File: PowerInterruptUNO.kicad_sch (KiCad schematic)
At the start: 47 parts, among them J1 Power, J10 6P6C, J11 USB_C_Receptacle_USB2.0, J12 Screw_Terminal_01x02, J13 USB_A, J14 Screw_Terminal_01x02, J2 Analog, J3 Barrel_Jack_Switch, J4 Screw_Terminal_01x06, J5 Screw_Terminal_01x06, J6 Screw_Terminal_01x03, J7 Screw_Terminal_01x02, J8 Digital/PWM, J9 Digital/PWM, Q1 MMBT3904, Q2 TIP42, U1 LM317_TO-220

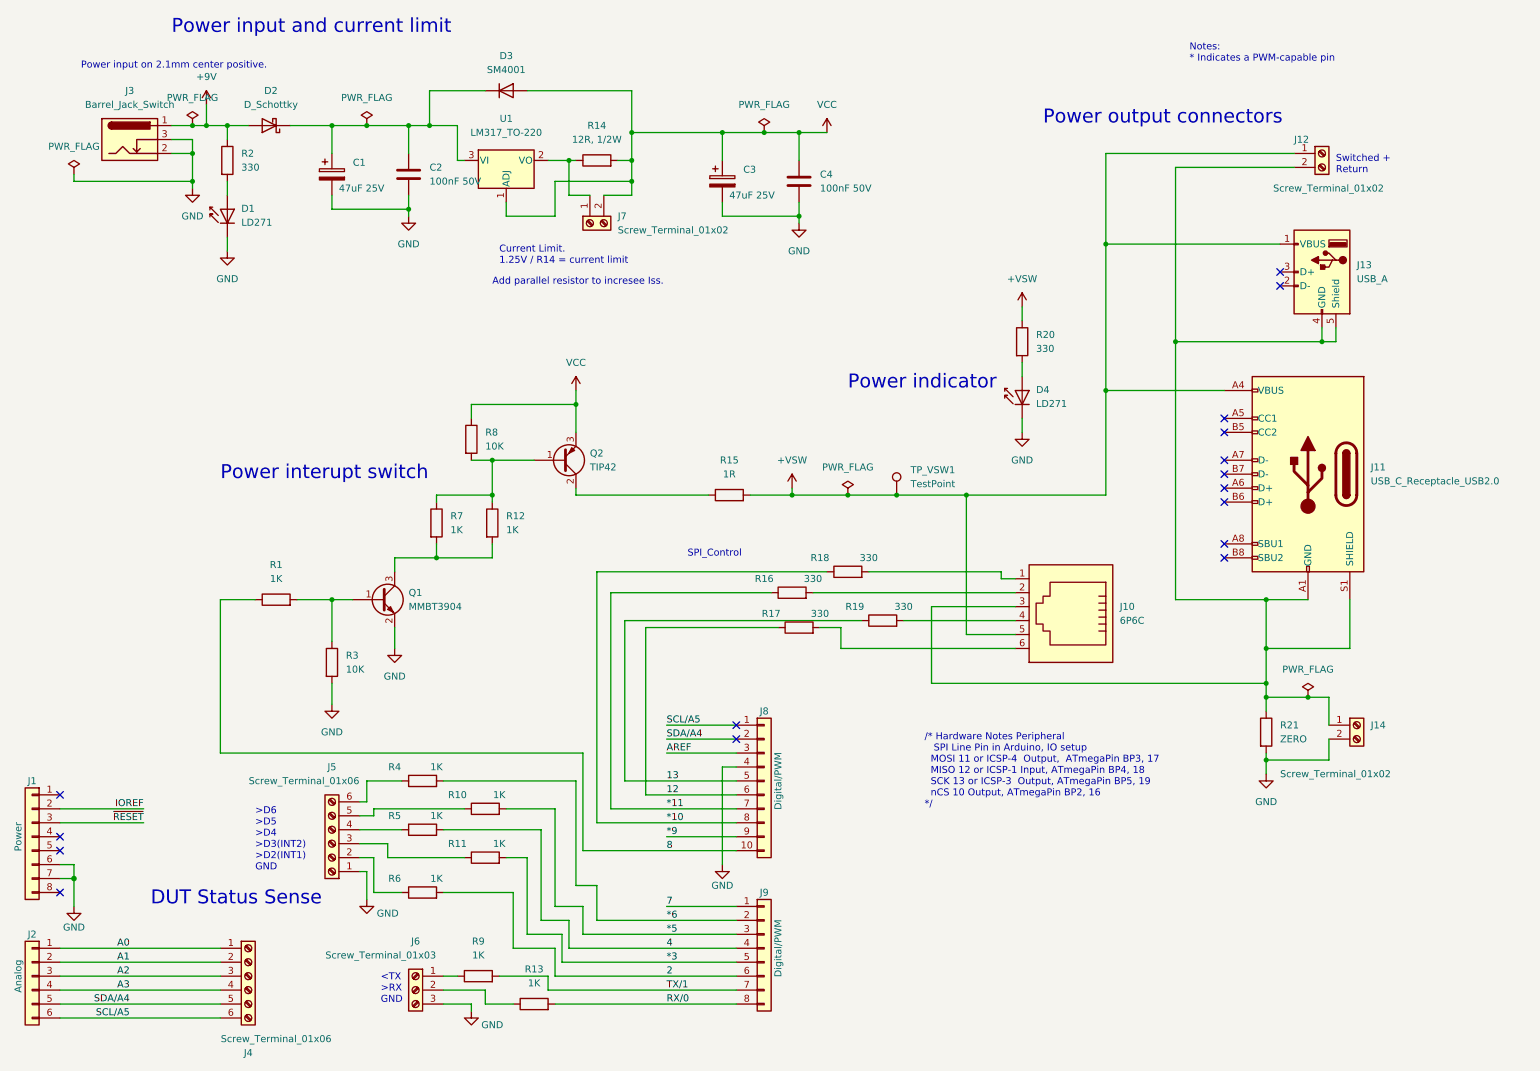
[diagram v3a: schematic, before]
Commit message: Add JLCPCB part numberes to some components.
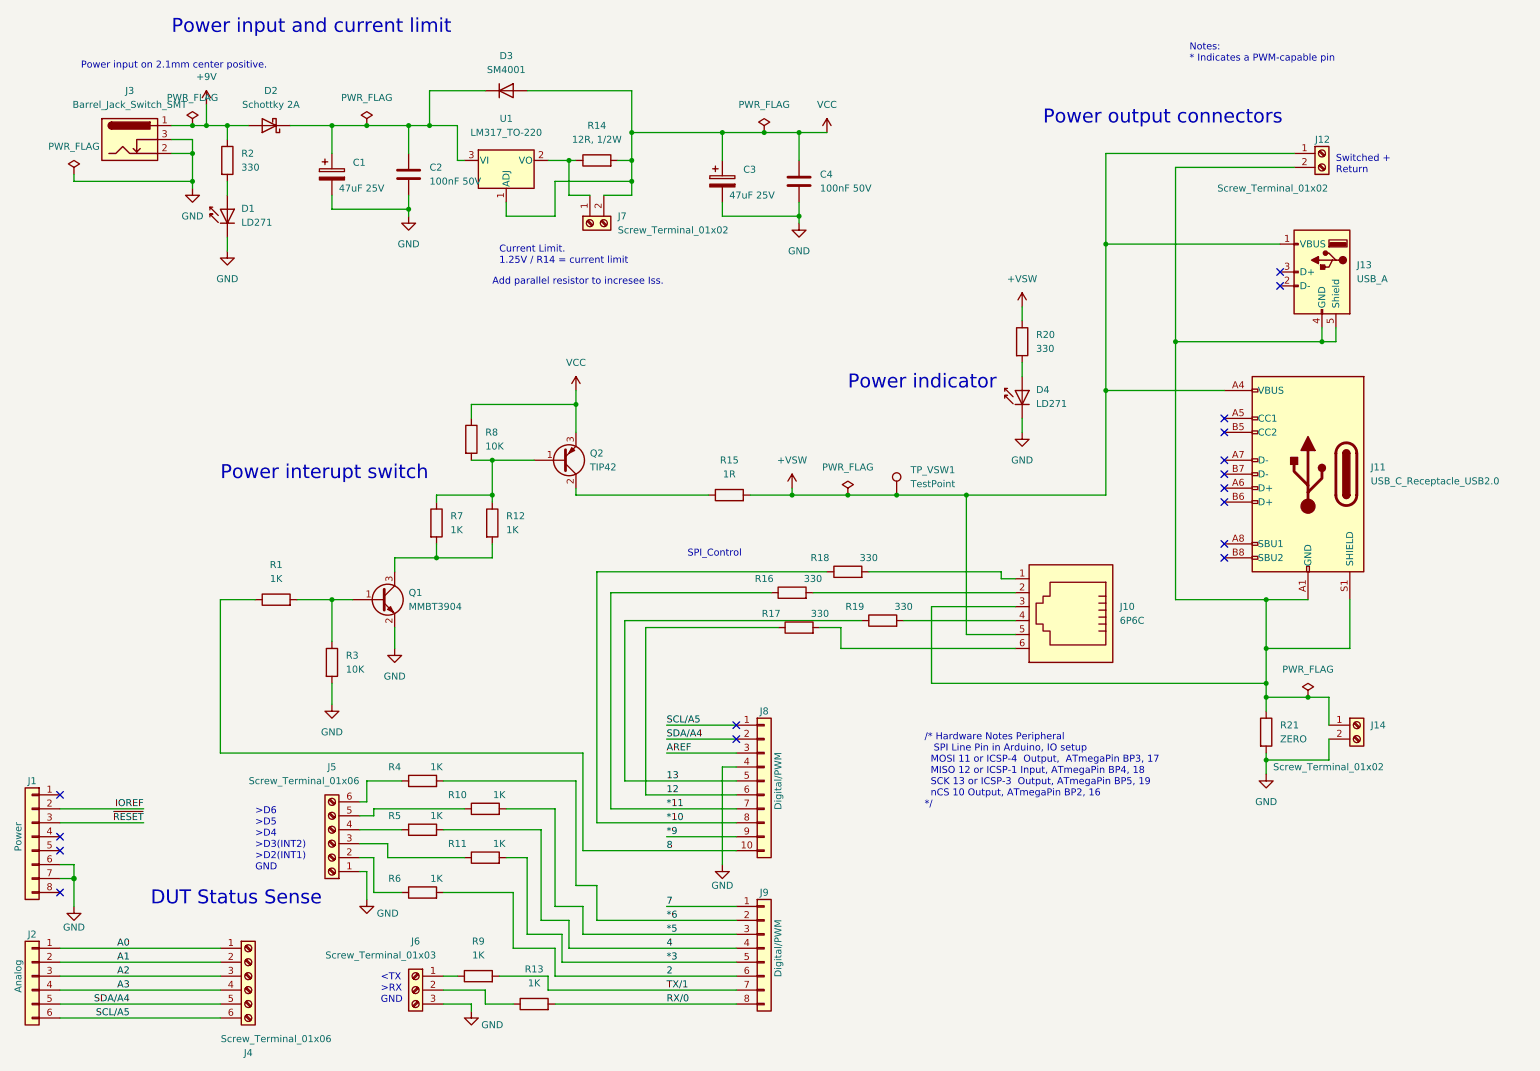
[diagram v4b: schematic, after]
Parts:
- C1, C3: Cost (none) -> 0.0357; Distributor 1 PN (none) -> C72521; MPN (none) -> RVT1E470M0605
- C2, C4: Cost (none) -> 0.0024; Distributor 1 PN (none) -> C14663
- D1: footprint LED_THT:LED_D5.0mm_IRGrey -> LED_SMD:LED_0603_1608Metric_Pad1.05x0.95mm_HandSolder; Cost (none) -> 0.0054; Distributor 1 (none) -> JLCPCB; Distributor 1 PN (none) -> C2286; MPN (none) -> KT-0603R; Manufacturer (none) -> Hubei KENTO Elec
- D2: value D_Schottky -> Schottky 2A; footprint (none) -> Diode_SMD:D_SMB; Cost (none) -> 0.0349; Distirbutor 1 PN (none) -> C14996; Distributor 1 (none) -> JLCPCB; Distributor 1 PN (none) -> C14996; MPN (none) -> SS210; Manufacturer (none) -> MDD（Microdiode Electronics）
- D3: Cost (none) -> 0.0672; Distirbutor 1 PN (none) -> C151781; Distributor 1 (none) -> JLCPCB; Distributor 1 PN (none) -> C151781; MPN (none) -> SM4001PL-TP; Manufacturer (none) -> MCC(Micro Commercial Components)
- D4: footprint LED_THT:LED_D5.0mm_IRGrey -> LED_SMD:LED_0603_1608Metric_Pad1.05x0.95mm_HandSolder; Cost (none) -> 0.0054; Distirbutor 1 PN (none) -> foo; Distributor 1 (none) -> JLCPCB; Distributor 1 PN (none) -> C2286; MPN (none) -> KT-0603R; Manufacturer (none) -> Hubei KENTO Elec
- J1, J10, J11, J13, J2, J4, J5, J6, J8, J9, R14, R21, TP_VSW1: Cost (none) -> foo; Distirbutor 1 PN (none) -> foo; Distributor 1 (none) -> JLCPCB; MPN (none) -> foo; Manufacturer (none) -> foo
- J12: footprint (none) -> TerminalBlock_TE-Connectivity:TerminalBlock_TE_282834-2_1x02_P2.54mm_Horizontal; Cost (none) -> 0.1686; Distirbutor 1 PN (none) -> foo; Distributor 1 (none) -> JLCPCB; Distributor 1 PN (none) -> C918120; MPN (none) -> DB125-2.54-2P-GN; Manufacturer (none) -> DIBO
- J14, J7: Cost (none) -> 0.1686; Distirbutor 1 PN (none) -> foo; Distributor 1 (none) -> JLCPCB; Distributor 1 PN (none) -> C918120; MPN (none) -> DB125-2.54-2P-GN; Manufacturer (none) -> DIBO
- J3: value Barrel_Jack_Switch -> Barrel_Jack_Switch_SMT; footprint (none) -> Connector_BarrelJack:BarrelJack_CLIFF_FC681465S_SMT_Horizontal; Cost (none) -> 0.205; Distributor 1 (none) -> JLCPCB; Distributor 1 PN (none) -> C319134; MPN (none) -> XKB Connectivity / Tensility International Corp; Manufacturer (none) -> DC-005-5A-2.0-SMT / 54-00164
- Q1: Cost (none) -> 0.0121; Distirbutor 1 PN (none) -> C20526; Distributor 1 (none) -> JLCPCB; Distributor 1 PN (none) -> C20526; MPN (none) -> MMBT3904; Manufacturer (none) -> Jiangsu Changjing Electronics Technology Co., Ltd.
- Q2: Cost (none) -> 0.2666; Distirbutor 1 PN (none) -> C92311; Distributor 1 (none) -> JLCPCB; MPN (none) -> TIP42C; Manufacturer (none) -> Jiangsu Changjing Electronics Technology Co., Ltd.
- R1, R10, R11, R12, R13, R4, R5, R6, R7, R9: Cost (none) -> 0.0012; Distirbutor 1 PN (none) -> C22548; Distributor 1 (none) -> JLCPCB; Distributor 1 PN (none) -> C22548; MPN (none) -> RC0603FR-071KL; Manufacturer (none) -> YAGEO
- R15: Cost (none) -> foo; Distributor 1 (none) -> JLCPCB; MPN (none) -> foo; Manufacturer (none) -> foo
- R16, R17, R18, R19, R2, R20: Cost (none) -> 0.0014; Distirbutor 1 PN (none) -> C105881; Distributor 1 (none) -> JLCPCB; Distributor 1 PN (none) -> C105881; MPN (none) -> RC0603FR-07330RL; Manufacturer (none) -> YAGEO
- R3, R8: Cost (none) -> 0.001; Distirbutor 1 PN (none) -> empty; Distributor 1 (none) -> JLCPCB; Distributor 1 PN (none) -> C99198; MPN (none) -> RC0603JR-0710KL; Manufacturer (none) -> YAGEO
- U1: Cost (none) -> foo; Distirbutor 1 PN (none) -> C88008; Distributor 1 PN C88008 -> (none)

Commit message: Add JLCPCB part numberes to some components.
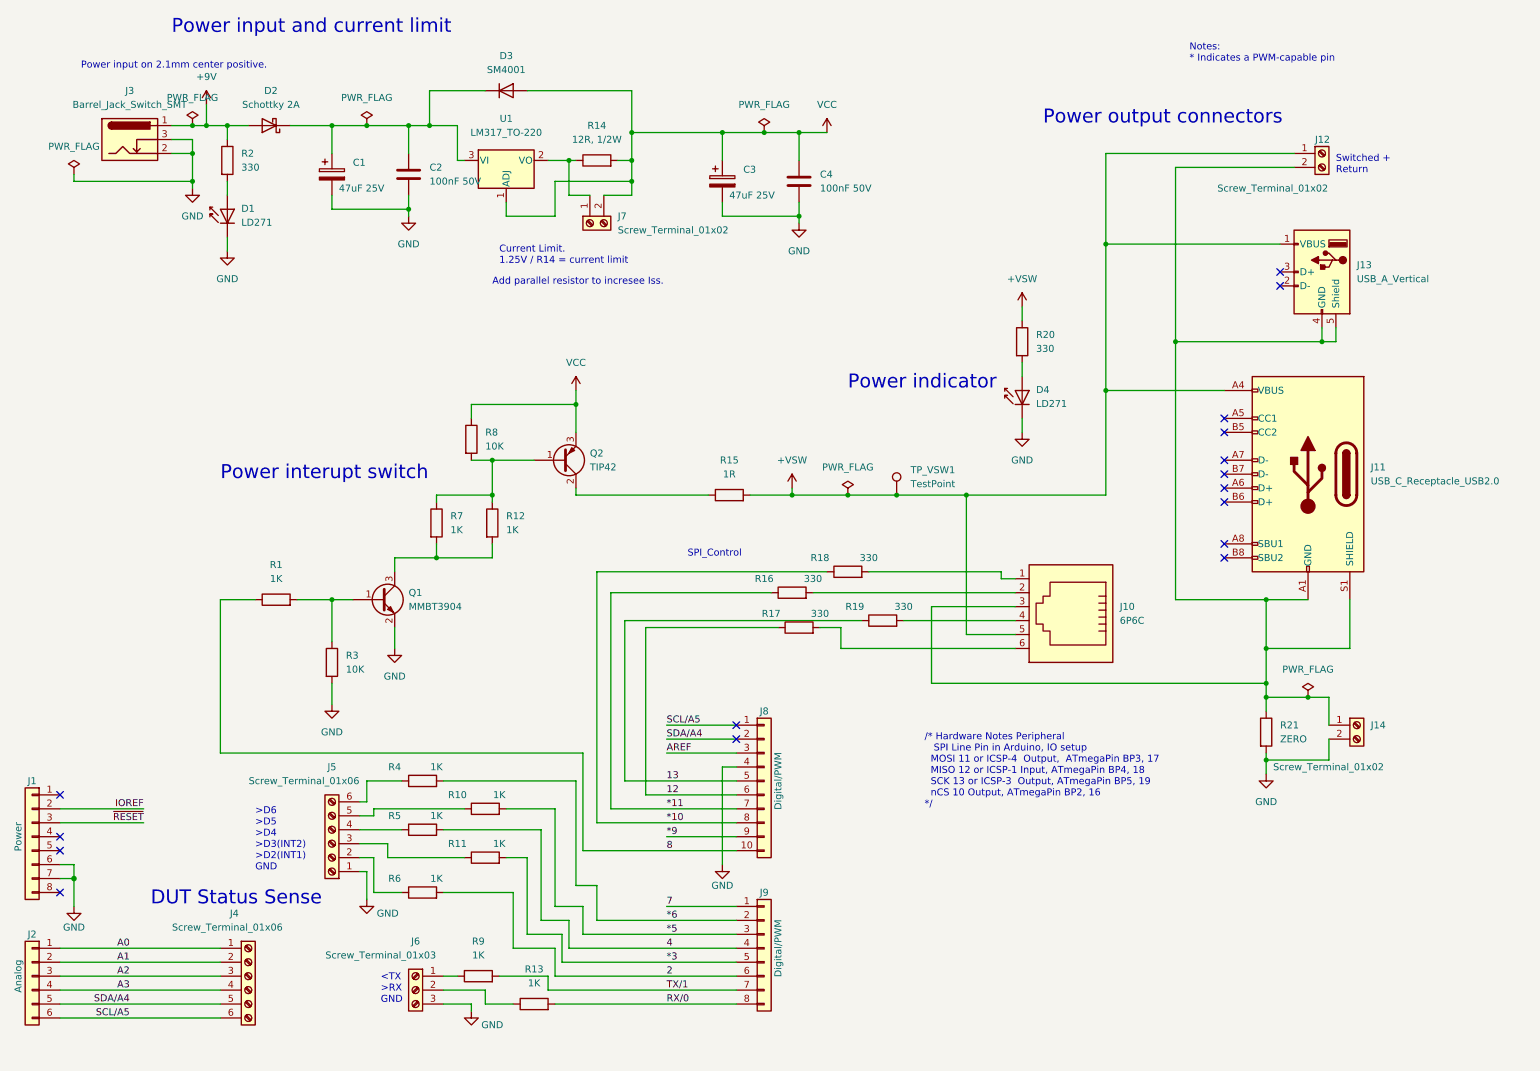
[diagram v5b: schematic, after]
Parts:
- J10: footprint (none) -> Connector_RJ:RJ12_Amphenol_54601; Cost foo -> 0.8546; Distributor 1 PN (none) -> C305981; MPN foo -> 5555165-1; Manufacturer foo -> TE Connectivity
- J11: footprint (none) -> Connector_USB:USB_C_Receptacle_XKB_U262-16XN-4BVC11; Cost foo -> 0.3344; Distributor 1 PN (none) -> C319148; MPN foo -> U262-161N-4BVC11; Manufacturer foo -> XKB Connectivity
- J13: value USB_A -> USB_A_Vertical; footprint (none) -> Connector_USB:USB_A_Wuerth_614004134726_Horizontal; Cost foo -> 0.1616; Distributor 1 PN (none) -> C26235; MPN foo -> C26235; Manufacturer foo -> Jing Extension of the Electronic Co.
- J4, J5: footprint (none) -> TerminalBlock_TE-Connectivity:TerminalBlock_TE_282834-6_1x06_P2.54mm_Horizontal; Cost foo -> 0.4798; Distributor 1 PN (none) -> C918124; MPN foo -> DB125-2.54-6P-GN; Manufacturer foo -> DIBO
- J6: footprint (none) -> TerminalBlock_TE-Connectivity:TerminalBlock_TE_282834-3_1x03_P2.54mm_Horizontal; Cost foo -> 0.2529; Distributor 1 PN (none) -> C918121; MPN foo -> DB125-2.54-3P-GN; Manufacturer foo -> DIBO

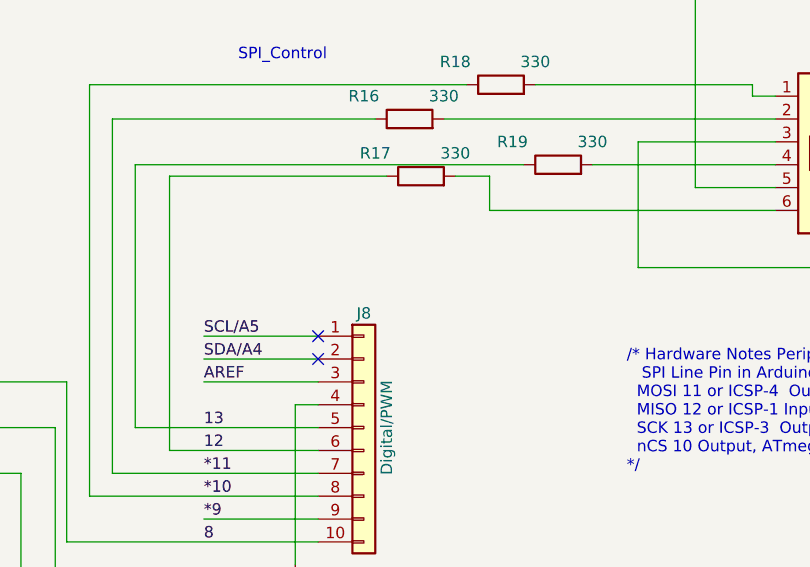
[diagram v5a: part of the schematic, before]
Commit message: Initial routing. 100% connected but lots of DRC errors to track down.
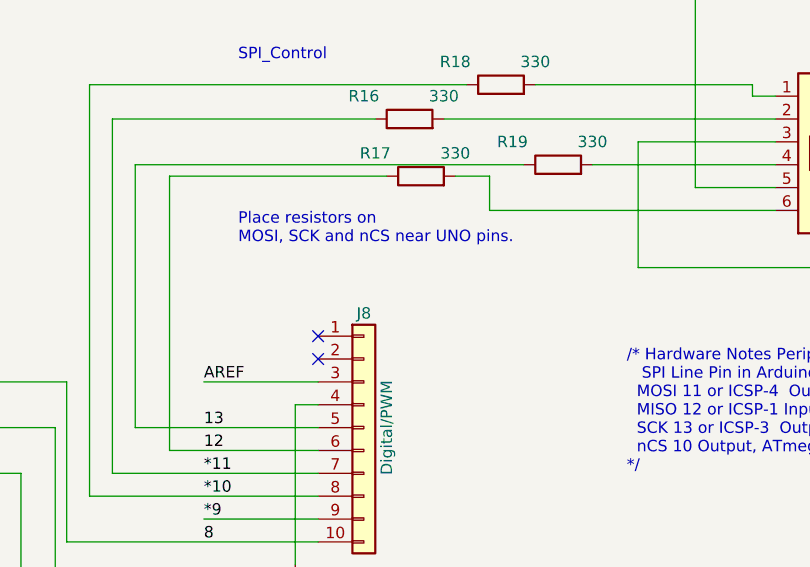
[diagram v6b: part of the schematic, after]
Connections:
- net SCL/A5: no longer J8.1 (Pin_1)
- net SDA/A4: no longer J8.2 (Pin_2)
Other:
- note added: "Place resistors on MOSI, SCK and nCS near UNO pins."
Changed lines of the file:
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@@
     (stroke (width 0) (type default) (color 0 0 0 0))
-  )
-  (wire (pts (xy 146.05 146.05) (xy 133.35 146.05))
-    (stroke (width 0) (type solid) (color 0 0 0 0))
   )
   (wire (pts (xy 53.34 57.15) (xy 53.34 59.69))
@@
   (wire (pts (xy 97.79 97.79) (xy 101.6 97.79))
     (stroke (width 0) (type default) (color 0 0 0 0))
-  )
-  (wire (pts (xy 146.05 148.59) (xy 133.35 148.59))
-    (stroke (width 0) (type solid) (color 0 0 0 0))
   )
   (wire (pts (xy 43.18 41.91) (xy 46.99 41.91))
@@
     (effects (font (size 2.54 2.54)) (justify left bottom))
   )
+  (text "Place resistors on\nMOSI, SCK and nCS near UNO pins."
+    (at 137.16 135.89 0)
+    (effects (font (size 1.27 1.27)) (justify left bottom))
+  )
   (text "Power indicator" (at 166.37 85.09 0)
     (effects (font (size 2.54 2.54)) (justify left bottom))
@@
     (effects (font (size 1.27 1.27)) (justify left bottom))
   )
-  (label "SDA{slash}A4" (at 133.35 148.59 0)
-    (effects (font (size 1.27 1.27)) (justify left bottom))
-  )
   (label "8" (at 133.35 168.91 0)
     (effects (font (size 1.27 1.27)) (justify left bottom))
@@
     (effects (font (size 1.27 1.27)) (justify left bottom))
   )
-  (label "SCL{slash}A5" (at 133.35 146.05 0)
-    (effects (font (size 1.27 1.27)) (justify left bottom))
-  )
